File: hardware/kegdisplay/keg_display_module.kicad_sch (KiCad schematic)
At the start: 15 parts, among them J1 RJ12_to_chain (either directi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, J2 RJ12_to_chain (either directi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, J3 OLED_SSD1306_I2C (confirm pin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, Q1 AO3401A, U1 MAX485, U2 Arduino Nano (socketed, not s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

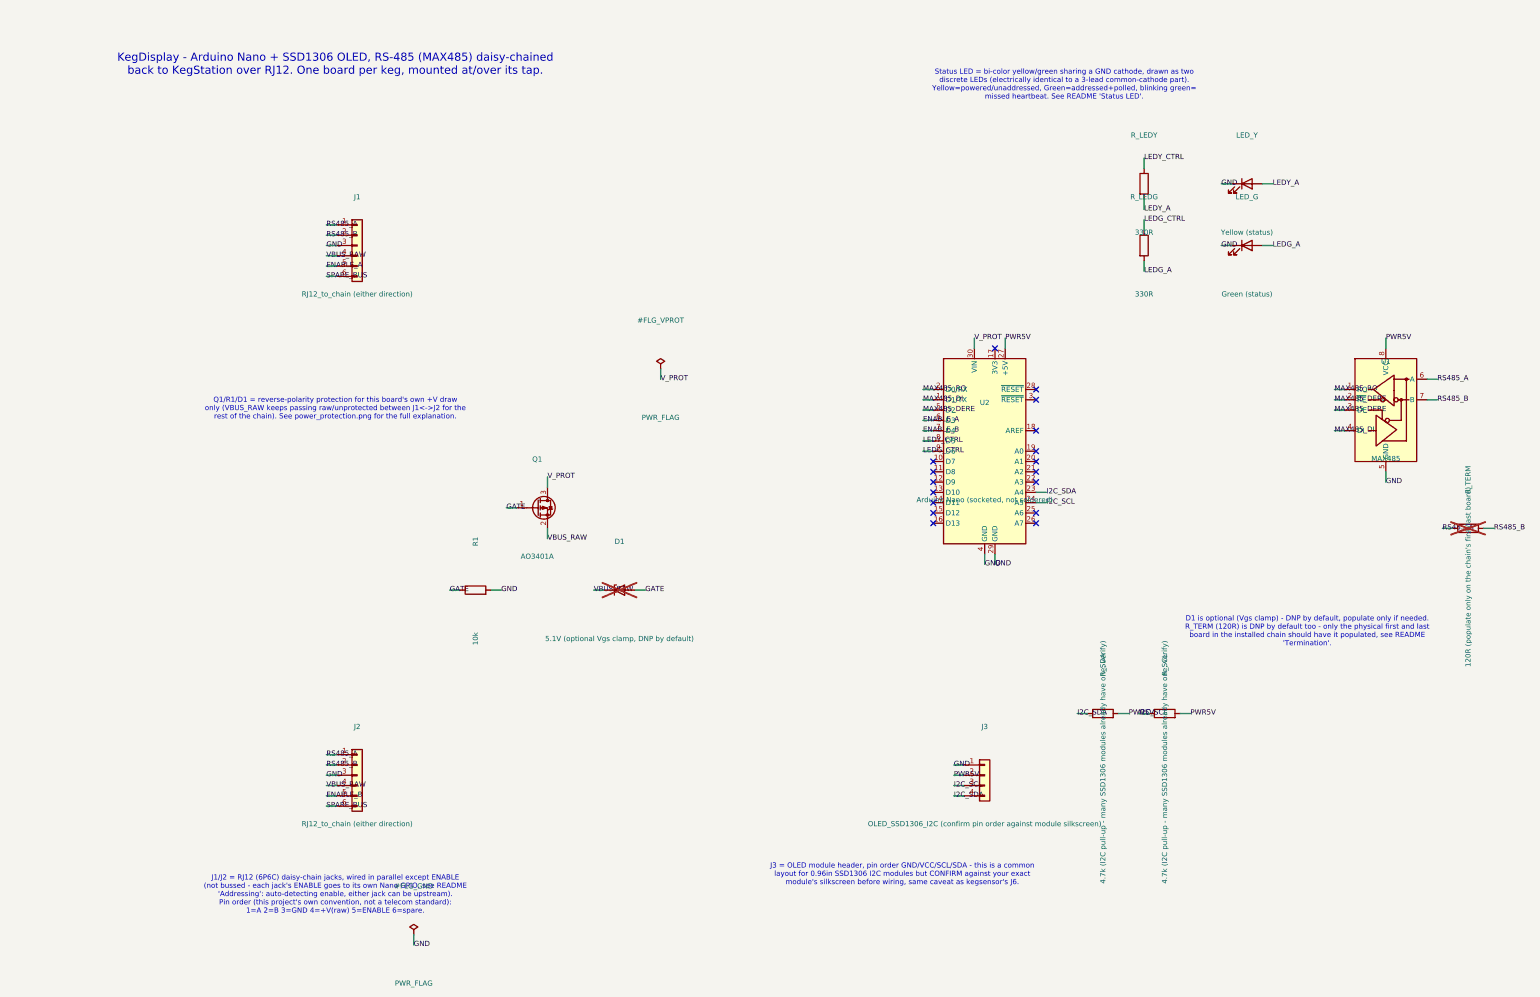
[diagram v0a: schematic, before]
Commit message: KegDisplay: settle on vertical off-the-shelf WS2812 strip, drop custom PCB
Went through several revisions this session: ATtiny1614+OLED per tap
(dropped - never fit the real ~100mm/~30mm mounting-space constraints
no matter how the board/connectors were arranged), then a custom
horizontal WS2812 LED-bar PCB (kept in this directory as generate_pcb.py/
generate_schematic.py, DRC-clean, but superseded), and finally a vertical
off-the-shelf LED strip mounted on the collar's side (~50x130mm
available there) - no custom PCB needed, and a vertical fill bar reads
more intuitively than a horizontal one.

Also adds the lid-module KiCad project (OLED + status LED carrier for
the now-superseded revision 4) and the case.scad/STL files from earlier
session work, none previously committed.

Co-Authored-By: Claude Sonnet 5 <noreply@anthropic.com>
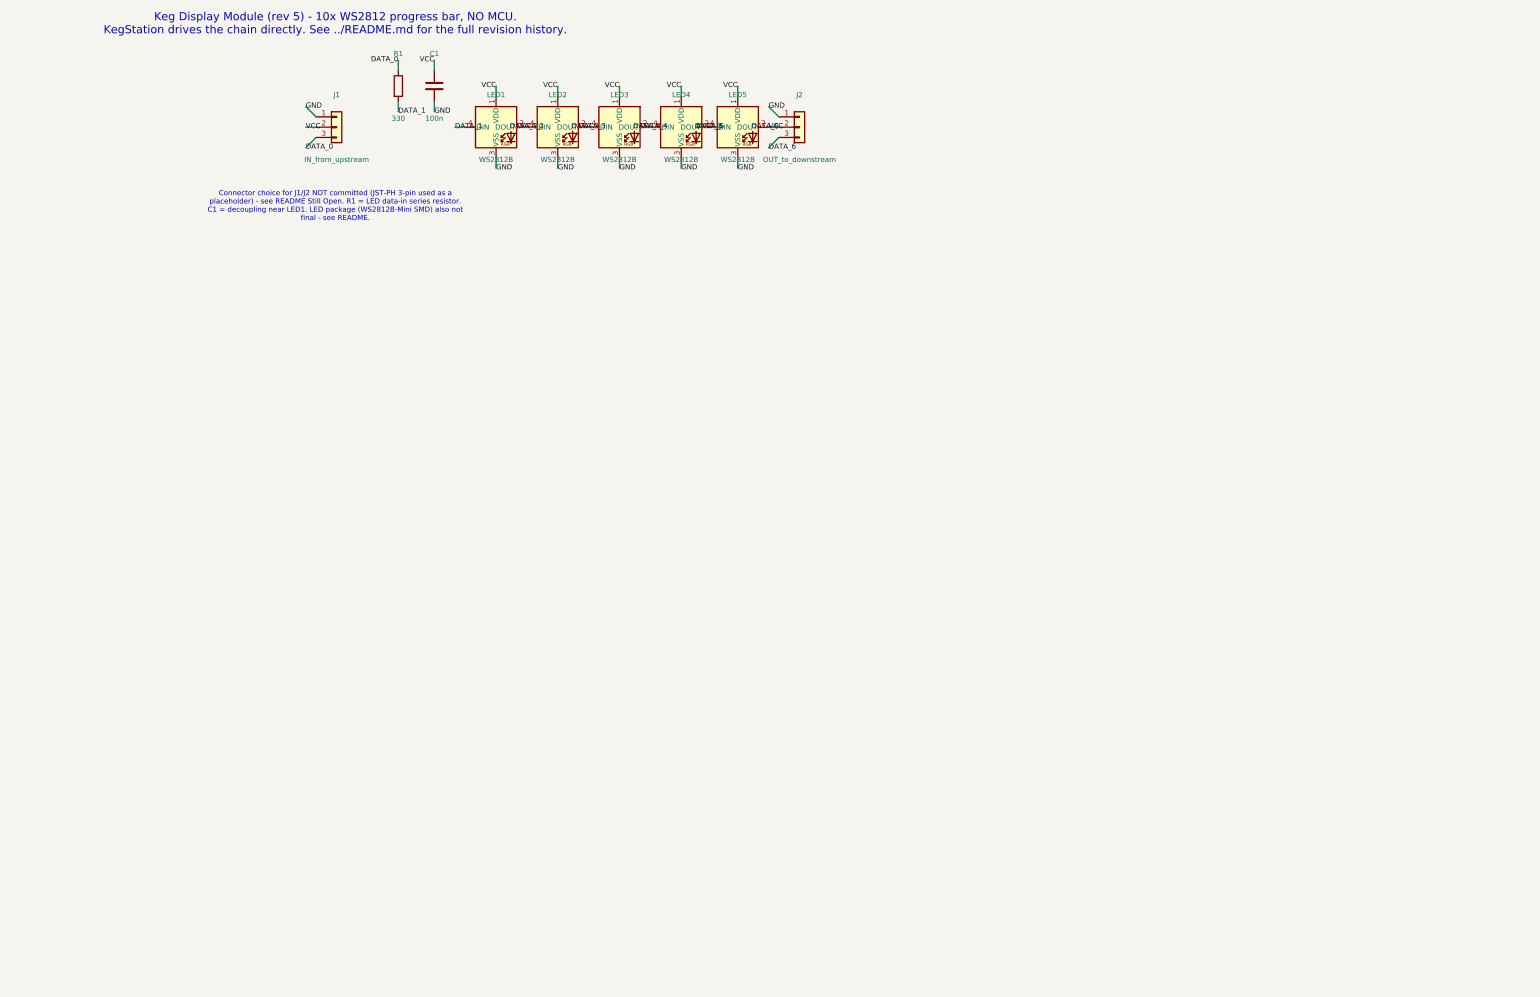
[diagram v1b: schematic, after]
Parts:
- removed D1: 5.1V (optional Vgs clamp, DNP by default), Diode_THT:D_DO-35_SOD27_P7.62mm_Horizontal, symbol Device:D_Zener
- removed J1, J2: RJ12_to_chain (either direction), Connector_RJ:RJ12_Amphenol_54601-x06_Horizontal, symbol Connector_Generic:Conn_01x06
- removed J3: OLED_SSD1306_I2C (confirm pin order against modul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, Connector_PinSocket_2.54mm:PinSocket_1x04_P2.54mm_Vertical, symbol Connector_Generic:Conn_01x04
- removed LED_G: Green (status), LED_THT:LED_D5.0mm, symbol Device:LED
- removed LED_Y: Yellow (status), LED_THT:LED_D5.0mm, symbol Device:LED
- removed Q1: AO3401A, Package_TO_SOT_SMD:SOT-23, symbol Transistor_FET:AO3401A
- removed R_LEDG, R_LEDY: 330R, Resistor_THT:R_Axial_DIN0207_L6.3mm_D2.5mm_P10.16mm_Horizontal, symbol Device:R
- removed R_SCL, R_SDA: 4.7k (I2C pull-up - many SSD1306 modules already 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, Resistor_THT:R_Axial_DIN0207_L6.3mm_D2.5mm_P10.16mm_Horizontal, symbol Device:R
- removed R_TERM: 120R (populate only on the chain's first/last boa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, Resistor_THT:R_Axial_DIN0207_L6.3mm_D2.5mm_P10.16mm_Horizontal, symbol Device:R
- removed U1: MAX485, Package_DIP:DIP-8_W7.62mm, symbol Interface_UART:MAX485
- removed U2: Arduino Nano (socketed, not soldered), Module:Arduino_Nano, symbol MCU_Module:Arduino_Nano_v2.x
- added C1: 100n, Capacitor_THT:C_Disc_D3.0mm_W2.0mm_P2.50mm, symbol Device:C
- added J1: IN_from_upstream, Connector_JST:JST_PH_B3B-PH-K_1x03_P2.00mm_Vertical, symbol Connector_Generic:Conn_01x03
- added J2: OUT_to_downstream, Connector_JST:JST_PH_B3B-PH-K_1x03_P2.00mm_Vertical, symbol Connector_Generic:Conn_01x03
- added LED1, LED2, LED3, LED4, LED5: WS2812B, LED_SMD:LED_WS2812B-Mini_PLCC4_3.5x3.5mm, symbol LED:WS2812B
- R1: value 10k -> 330; footprint Resistor_THT:R_Axial_DIN0207_L6.3mm_D2.5mm_P10.16mm_Horizontal -> Resistor_THT:R_Axial_DIN0207_L6.3mm_D2.5mm_P2.54mm_Vertical
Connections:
- net GND: now also C1.2, J1.1 (Pin_1), J2.1 (Pin_1), LED1.3 (VSS), LED2.3 (VSS), LED3.3 (VSS), LED4.3 (VSS), LED5.3 (VSS); no longer R1.2
- net GATE renamed DATA_0
- net DATA_0: now also J1.3 (Pin_3)
- new net DATA_1: LED1.4 (DIN), R1.2
- new net DATA_2: LED1.2 (DOUT), LED2.4 (DIN)
- new net DATA_3: LED2.2 (DOUT), LED3.4 (DIN)
- new net DATA_4: LED3.2 (DOUT), LED4.4 (DIN)
- new net DATA_5: LED4.2 (DOUT), LED5.4 (DIN)
- new net DATA_6: C1.1, J1.2 (Pin_2), J2.2 (Pin_2), J2.3 (Pin_3), LED1.1 (VDD), LED2.1 (VDD), LED3.1 (VDD), LED4.1 (VDD), LED5.1 (VDD), LED5.2 (DOUT)
- no-connect marks 17 -> 0
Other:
- note added: "Connector choice for J1/J2 NOT committed (JST-PH 3-pin used as a placeholder) - see README Still Open. R1 = LED data-in series resistor. C1 = decoupling near LED1. LED package (WS2812B-Mini SMD) also not final - see README."
- note added: "Keg Display Module (rev 5) - 10x WS2812 progress bar, NO MCU. KegStation drives the chain directly. See ../README.md for the full revision history."
- note removed: "D1 is optional (Vgs clamp) - DNP by default, populate only if needed. R_TERM (120R) is DNP by default too - only the physical first and last board in the installed chain should have it populated, see README 'Termination'."
- note removed: "J1/J2 = RJ12 (6P6C) daisy-chain jacks, wired in parallel except ENABLE (not bussed - each jack's ENABLE goes to its own Nano GPIO, see README 'Addressing': auto-detecting enable, either jack can be upstream). Pin order (this project's own convention, not a telecom standard): 1=A 2=B 3=GND 4=+V(raw) 5=ENABLE 6=spare."
- note removed: "J3 = OLED module header, pin order GND/VCC/SCL/SDA - this is a common layout for 0.96in SSD1306 I2C modules but CONFIRM against your exact module's silkscreen before wiring, same caveat as kegsensor's J6."
- note removed: "KegDisplay - Arduino Nano + SSD1306 OLED, RS-485 (MAX485) daisy-chained back to KegStation over RJ12. One board per keg, mounted at/over its tap."
- note removed: "Q1/R1/D1 = reverse-polarity protection for this board's own +V draw only (VBUS_RAW keeps passing raw/unprotected between J1<->J2 for the rest of the chain). See power_protection.png for the full explanation."
- note removed: "Status LED = bi-color yellow/green sharing a GND cathode, drawn as two discrete LEDs (electrically identical to a 3-lead common-cathode part). Yellow=powered/unaddressed, Green=addressed+polled, blinking green= missed heartbeat. See README 'Status LED'."
